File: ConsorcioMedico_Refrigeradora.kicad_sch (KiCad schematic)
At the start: 46 parts, among them J1 BatteryHolder, J37 SWD, J5 AC, J5 USART, J6 Screw_Terminal_01x01, J7 Screw_Terminal_01x01, J8 AC, U1 STM32F411RETx, U2 AP63205WU, U3 LDL1117, U9 HLK-PMx

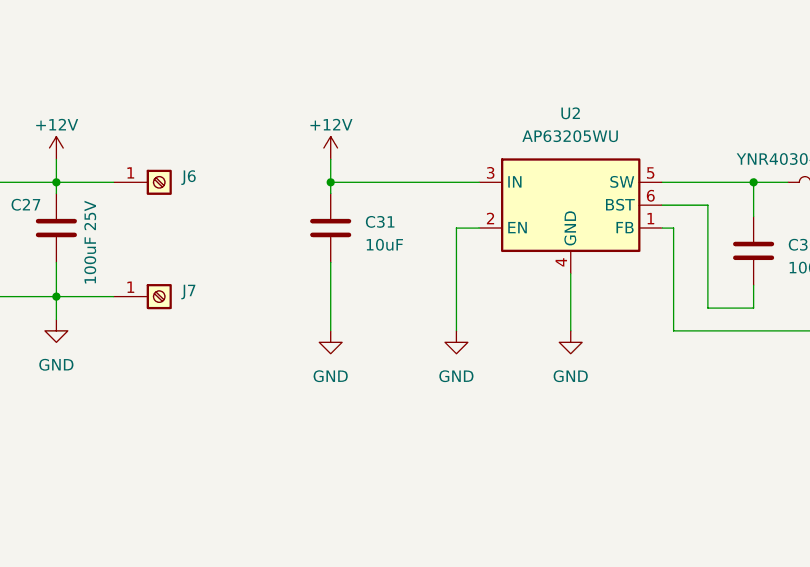
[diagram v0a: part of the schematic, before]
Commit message: SCH: pin EN se corrige para activar la alimentación de 5V, se cambia el empaquetado de varias resistencias 0603 a 0805. PCB: Se alarga el plano de GND, se acomodan los componentes 0805, se completa de colocar la serigrafía, se ensancha la pista de AC. JLCPCB: Se actualiza
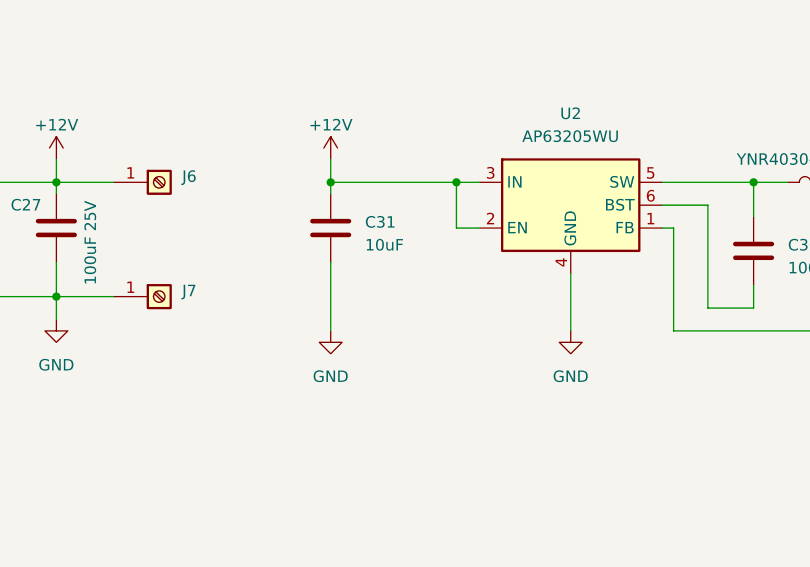
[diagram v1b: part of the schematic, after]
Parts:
- R24, R29: footprint 1-Resistor:R_0603_1608Metric -> 1-Resistor:R_0805_2012Metric
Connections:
- net +12V: now also U2.2 (EN)
- net GND: no longer U2.2 (EN)
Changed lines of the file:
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@@
   (junction (at 492.76 228.6) (diameter 0) (color 0 0 0 0)
+  )
+  (junction (at 149.86 68.58) (diameter 0) (color 0 0 0 0)
   )
   (junction (at 552.45 66.04) (diameter 0) (color 0 0 0 0)
@@
     (stroke (width 0) (type default))
   )
-  (wire (pts (xy 152.4 68.58) (xy 135.89 68.58))
+  (wire (pts (xy 152.4 68.58) (xy 149.86 68.58))
     (stroke (width 0) (type default))
   )
@@
     (stroke (width 0) (type default))
   )
+  (wire (pts (xy 149.86 68.58) (xy 135.89 68.58))
+    (stroke (width 0) (type default))
+  )
   (wire (pts (xy 392.43 54.61) (xy 394.97 54.61))
     (stroke (width 0) (type default))
@@
     (stroke (width 0) (type default))
   )
+  (wire (pts (xy 149.86 68.58) (xy 149.86 73.66))
+    (stroke (width 0) (type default))
+  )
   (wire (pts (xy 172.72 68.58) (xy 182.88 68.58))
     (stroke (width 0) (type default))
@@
   )
   (wire (pts (xy 336.55 124.46) (xy 377.19 124.46))
-    (stroke (width 0) (type default))
-  )
-  (wire (pts (xy 149.86 73.66) (xy 149.86 85.09))
     (stroke (width 0) (type default))
   )
@@
         (path "/e86bbed0-5bdc-4982-8297-fb5cecea731c"
           (reference "#PWR02") (unit 1)
-        )
-      )
-    )
-  )
-  (symbol (lib_id "power:GND") (at 149.86 85.09 0) (unit 1)
-    (in_bom yes) (on_board yes) (dnp no) (fields_autoplaced)
-    (property "Reference" "#PWR?" (at 149.86 91.44 0)
-      (effects (font (size 1.27 1.27)) hide)
-    )
-    (property "Value" "GND" (at 149.86 90.17 0)
-      (effects (font (size 1.27 1.27)))
-    )
-    (property "Footprint" "" (at 149.86 85.09 0)
-      (effects (font (size 1.27 1.27)) hide)
-    )
-    (property "Datasheet" "" (at 149.86 85.09 0)
-      (effects (font (size 1.27 1.27)) hide)
-    )
-    (pin "1")
-    (instances
-      (project "Sensor_v3_Mirror"
-        (path "/2d53403b-ed0e-48ec-9a21-e8ff6d03c1a6"
-          (reference "#PWR?") (unit 1)
-        )
-      )
-      (project "STM32_Esterilizador"
-        (path "/2e4bcfd0-2bd9-4947-aec4-3d35e12c1f92"
-          (reference "#PWR017") (unit 1)
-        )
-      )
-      (project "ConsorcioMedico_Refrigeradora"
-        (path "/e86bbed0-5bdc-4982-8297-fb5cecea731c"
-          (reference "#PWR095") (unit 1)
         )
       )
@@
       (effects (font (size 1.27 1.27)) (justify right))
     )
-    (property "Footprint" "1-Resistor:R_0603_1608Metric" (at 494.538 218.44 90)
+    (property "Footprint" "1-Resistor:R_0805_2012Metric" (at 494.538 218.44 90)
       (effects (font (size 1.27 1.27)) hide)
     )
@@
       (effects (font (size 1.27 1.27)) (justify right))
     )
-    (property "Footprint" "1-Resistor:R_0603_1608Metric" (at 484.378 218.44 90)
-      (effects (font (size 1.27 1.27)) hide)
-    )
+    (property "Footprint" "1-Resistor:R_0805_2012Metric" (at 484.378 218.44 90)
+      (effects (font (size 1.27 1.27)) hide)
+    )

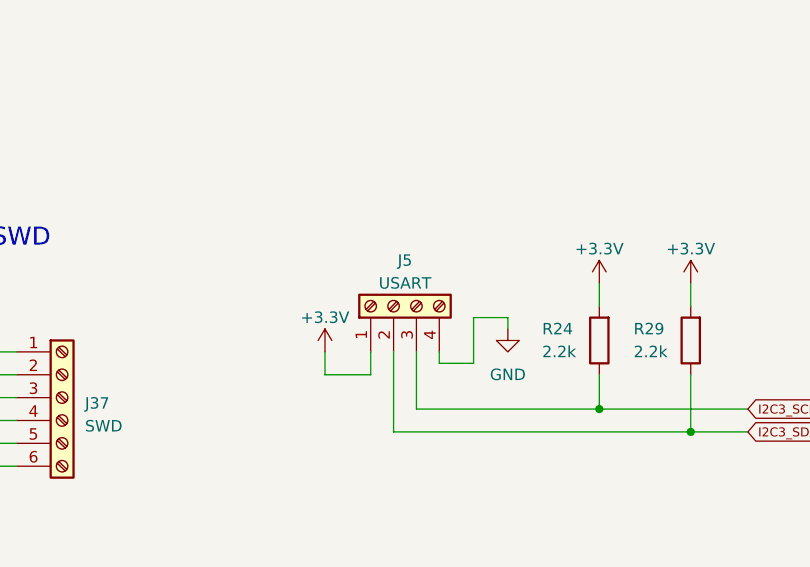
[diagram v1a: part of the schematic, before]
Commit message: Placa_v2: Version de la tarjeta añadiendo 3 leds al costado derecho, se necesitará mover fuente de poder y acomodar. SCH: Se ha cambiado el nombre del conector USART a I2C
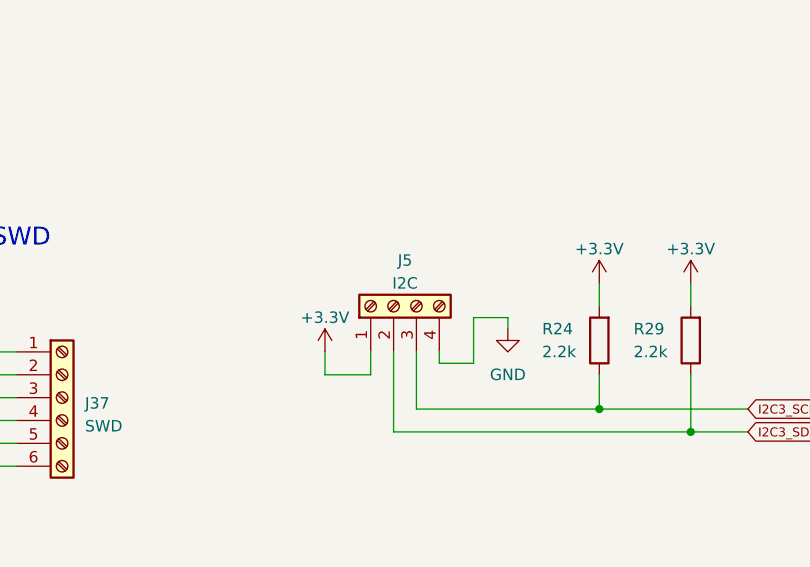
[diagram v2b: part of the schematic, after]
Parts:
- J5: value USART -> I2C
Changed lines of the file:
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@@
       (effects (font (size 1.27 1.27)))
     )
-    (property "Value" "USART" (at 461.01 212.09 90)
+    (property "Value" "I2C" (at 461.01 212.09 90)
       (effects (font (size 1.27 1.27)))
     )

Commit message: SCH
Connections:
- net Button_Cooling is gone; now on net Button_Light: U1.53 (PC12)
- net Button_Light: no longer U1.54 (PD2)
- net Led_Power_State: now reaches U1.27 (PB1)
- net Led_Button_Lock: now reaches U1.28 (PB2)
- net Led_Door_State: now reaches U1.29 (PB10)
- net Button_Buzzer renamed Button_Power
- net Button_Touch renamed Button_Set
- net LED_Defrost renamed Led_Cooling_State
- net LED_Door renamed Led_Defroting_State
- net LED_Status renamed Led_Status
- net LED_TempAlarm renamed Led_Fan_State
- new net Button_Sound: U1.54 (PD2)
- no-connect marks 5 -> 2
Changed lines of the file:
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@@
   (junction (at 513.08 77.47) (diameter 0) (color 0 0 0 0)
   )
-  (no_connect (at 412.75 109.22))
-  (no_connect (at 412.75 132.08))
   (no_connect (at 377.19 119.38))
   (no_connect (at 412.75 101.6))
-  (no_connect (at 412.75 111.76))
   (polyline (pts (xy 430.53 143.51) (xy 431.8 143.51))
     (stroke (width 0) (type default))
@@
     (stroke (width 0) (type default))
   )
-  (polyline (pts (xy 429.26 130.81) (xy 430.53 130.81))
+  (polyline (pts (xy 431.8 130.81) (xy 433.07 130.81))
     (stroke (width 0) (type default))
   )
@@
     (stroke (width 0) (type default))
   )
+  (wire (pts (xy 435.61 132.08) (xy 412.75 132.08))
+    (stroke (width 0) (type default))
+  )
   (wire (pts (xy 331.47 67.31) (xy 334.01 67.31))
     (stroke (width 0) (type default))
@@
     (stroke (width 0) (type default))
   )
-  (polyline (pts (xy 429.26 120.65) (xy 430.53 120.65))
+  (polyline (pts (xy 431.8 120.65) (xy 433.07 120.65))
     (stroke (width 0) (type default))
   )
@@
     (stroke (width 0) (type default))
   )
+  (wire (pts (xy 435.61 111.76) (xy 412.75 111.76))
+    (stroke (width 0) (type default))
+  )
   (wire (pts (xy 367.03 81.28) (xy 377.19 81.28))
     (stroke (width 0) (type default))
@@
     (stroke (width 0) (type default))
   )
+  (wire (pts (xy 435.61 109.22) (xy 412.75 109.22))
+    (stroke (width 0) (type default))
+  )
   (wire (pts (xy 39.37 68.58) (xy 50.8 68.58))
     (stroke (width 0) (type default))
@@
     (stroke (width 0) (type default))
   )
-  (polyline (pts (xy 430.53 130.81) (xy 430.53 120.65))
+  (polyline (pts (xy 433.07 130.81) (xy 433.07 120.65))
     (stroke (width 0) (type default))
   )
@@
     (stroke (width 0) (type default))
   )
-  (text "SWD" (at 419.1 113.03 0)
+  (text "SWD" (at 423.6955 114.9772 0)
     (effects (font (size 1.27 1.27)) (justify right bottom))
   )
@@
     (effects (font (size 5 5) (thickness 1) bold) (justify left bottom))
   )
-  (text "LED" (at 434.34 127 0)
+  (text "LED" (at 436.88 127 0)
     (effects (font (size 1.27 1.27)) (justify right bottom))
   )
@@
     (effects (font (size 1.27 1.27)) (justify right bottom))
   )
-  (text "Relay" (at 429.26 107.95 0)
+  (text "Relay" (at 428.16 107.6862 0)
     (effects (font (size 1.27 1.27)) (justify right bottom))
   )
@@
     )
   )
-  (global_label "Button_Touch" (shape input) (at 374.65 106.68 180) (fields_autoplaced)
-    (effects (font (size 1 1)) (justify right))
-    (property "Intersheetrefs" "${INTERSHEET_REFS}" (at 362.4096 106.68 0)
-      (effects (font (size 1.27 1.27)) (justify right) hide)
-    )
-  )
   (global_label "MCU_TX1" (shape input) (at 439.42 86.36 0) (fields_autoplaced)
     (effects (font (size 1 1)) (justify left))
@@
     )
   )
+  (global_label "Button_Power" (shape input) (at 374.65 104.14 180) (fields_autoplaced)
+    (effects (font (size 1 1)) (justify right))
+    (property "Intersheetrefs" "${INTERSHEET_REFS}" (at 362.3145 104.14 0)
+      (effects (font (size 1.27 1.27)) (justify right) hide)
+    )
+  )
   (global_label "SWDIO" (shape input) (at 414.02 227.33 180) (fields_autoplaced)
     (effects (font (size 1 1)) (justify right))
@@
     )
   )
-  (global_label "Button_Buzzer" (shape input) (at 374.65 104.14 180) (fields_autoplaced)
-    (effects (font (size 1 1)) (justify right))
-    (property "Intersheetrefs" "${INTERSHEET_REFS}" (at 361.7431 104.14 0)
+  (global_label "Button_Sound" (shape input) (at 367.03 81.28 180) (fields_autoplaced)
+    (effects (font (size 1 1)) (justify right))
+    (property "Intersheetrefs" "${INTERSHEET_REFS}" (at 354.5514 81.28 0)
       (effects (font (size 1.27 1.27)) (justify right) hide)
     )
@@
     )
   )
-  (global_label "LED_TempAlarm" (shape input) (at 414.02 124.46 0) (fields_autoplaced)
-    (effects (font (size 1 1)) (justify left))
-    (property "Intersheetrefs" "${INTERSHEET_REFS}" (at 427.8792 124.46 0)
-      (effects (font (size 1.27 1.27)) (justify left) hide)
-    )
-  )
-  (global_label "LED_Door" (shape input) (at 414.02 127 0) (fields_autoplaced)
-    (effects (font (size 1 1)) (justify left))
-    (property "Intersheetrefs" "${INTERSHEET_REFS}" (at 423.2127 127 0)
+  (global_label "Led_Defroting_State" (shape input) (at 414.02 127 0) (fields_autoplaced)
+    (effects (font (size 1 1)) (justify left))
+    (property "Intersheetrefs" "${INTERSHEET_REFS}" (at 431.0697 127 0)
       (effects (font (size 1.27 1.27)) (justify left) hide)
     )
@@
     )
   )
+  (global_label "Led_Button_Lock" (shape input) (at 435.61 111.76 0) (fields_autoplaced)
+    (effects (font (size 1 1)) (justify left))
+    (property "Intersheetrefs" "${INTERSHEET_REFS}" (at 450.2312 111.76 0)
+      (effects (font (size 1.27 1.27)) (justify left) hide)
+    )
+  )
+  (global_label "Led_Power_State" (shape input) (at 435.61 109.22 0) (fields_autoplaced)
+    (effects (font (size 1 1)) (justify left))
+    (property "Intersheetrefs" "${INTERSHEET_REFS}" (at 450.2787 109.22 0)
+      (effects (font (size 1.27 1.27)) (justify left) hide)
+    )
+  )
   (global_label "SWCLK" (shape input) (at 414.02 222.25 180) (fields_autoplaced)
     (effects (font (size 1 1)) (justify right))
@@
     )
   )
+  (global_label "Led_Cooling_State" (shape input) (at 414.02 129.54 0) (fields_autoplaced)
+    (effects (font (size 1 1)) (justify left))
+    (property "Intersheetrefs" "${INTERSHEET_REFS}" (at 429.8794 129.54 0)
+      (effects (font (size 1.27 1.27)) (justify left) hide)
+    )
+  )
   (global_label "D" (shape input) (at 414.02 71.12 0) (fields_autoplaced)
     (effects (font (size 1 1)) (justify left))
@@
     )
   )
-  (global_label "LED_Defrost" (shape input) (at 414.02 129.54 0) (fields_autoplaced)
-    (effects (font (size 1 1)) (justify left))
-    (property "Intersheetrefs" "${INTERSHEET_REFS}" (at 425.1173 129.54 0)
-      (effects (font (size 1.27 1.27)) (justify left) hide)
-    )
-  )
   (global_label "RESET" (shape input) (at 360.68 48.26 180) (fields_autoplaced)
     (effects (font (size 1 1)) (justify right))
@@
     )
   )
+  (global_label "Led_Door_State" (shape input) (at 435.61 132.08 0) (fields_autoplaced)
+    (effects (font (size 1 1)) (justify left))
+    (property "Intersheetrefs" "${INTERSHEET_REFS}" (at 449.2788 132.08 0)
+      (effects (font (size 1.27 1.27)) (justify left) hide)
+    )
+  )
   (global_label "SWDIO" (shape input) (at 440.69 96.52 0) (fields_autoplaced)
     (effects (font (size 1 1)) (justify left))
@@
     )
   )
-  (global_label "Button_Light" (shape input) (at 367.03 81.28 180) (fields_autoplaced)
-    (effects (font (size 1 1)) (justify right))
-    (property "Intersheetrefs" "${INTERSHEET_REFS}" (at 355.4563 81.28 0)
-      (effects (font (size 1.27 1.27)) (justify right) hide)
-    )
-  )
   (global_label "I2C3_SCL" (shape input) (at 422.91 83.82 0) (fields_autoplaced)
     (effects (font (size 1 1)) (justify left))
@@
     )
   )
-  (global_label "LED_Status" (shape input) (at 414.02 121.92 0) (fields_autoplaced)
-    (effects (font (size 1 1)) (justify left))
-    (property "Intersheetrefs" "${INTERSHEET_REFS}" (at 424.4984 121.92 0)
+  (global_label "Led_Status" (shape input) (at 414.02 121.92 0) (fields_autoplaced)
+    (effects (font (size 1 1)) (justify left))
+    (property "Intersheetrefs" "${INTERSHEET_REFS}" (at 424.3555 121.92 0)
       (effects (font (size 1.27 1.27)) (justify left) hide)
     )
@@
     )
   )
+  (global_label "Button_Set" (shape input) (at 374.65 106.68 180) (fields_autoplaced)
+    (effects (font (size 1 1)) (justify right))
+    (property "Intersheetrefs" "${INTERSHEET_REFS}" (at 364.3621 106.68 0)
+      (effects (font (size 1.27 1.27)) (justify right) hide)
+    )
+  )
+  (global_label "Button_Light" (shape input) (at 367.03 116.84 180) (fields_autoplaced)
+    (effects (font (size 1 1)) (justify right))
+    (property "Intersheetrefs" "${INTERSHEET_REFS}" (at 355.4563 116.84 0)
+      (effects (font (size 1.27 1.27)) (justify right) hide)
+    )
+  )
   (global_label "USB_DM" (shape input) (at 415.29 91.44 0) (fields_autoplaced)
     (effects (font (size 1 1)) (justify left))
@@
     )
   )
-  (global_label "Button_Cooling" (shape input) (at 367.03 116.84 180) (fields_autoplaced)
-    (effects (font (size 1 1)) (justify right))
-    (property "Intersheetrefs" "${INTERSHEET_REFS}" (at 353.5038 116.84 0)
-      (effects (font (size 1.27 1.27)) (justify right) hide)
-    )
-  )
   (global_label "F" (shape input) (at 414.02 76.2 0) (fields_autoplaced)
     (effects (font (size 1 1)) (justify left))
@@
       (effects (font (size 1.27 1.27)) (justify left) hide)
     )
+  )
+  (global_label "Led_Fan_State" (shape input) (at 414.02 124.46 0) (fields_autoplaced)
+    (effects (font (size 1 1)) (justify left))
+    (property "Intersheetrefs" "${INTERSHEET_REFS}" (at 426.9269 124.46 0)
+      (effects (font (size 1.27 1.27)) (justify left) hide)
+    )

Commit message: Luego de modificaciones de Dandy
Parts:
- removed C8: 1uF 10V, 1-Capacitor:C_0805_2012Metric, symbol 1-Capacitor:C_0805
- added C13, C14, C34: 100nF 50V, 1-Capacitor:C_0603_1608Metric, symbol 1-Capacitor:C_0603
- renumbered J5 to J10, J8 to J19
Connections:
- net +12V: now also C34.1
- net +3.3V: now also C13.1
- net +5V: now also C14.1
- net GND: now also C13.2, C14.2, C34.2
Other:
- moved on the sheet: C31, C32, C33, C36, L3, U2
